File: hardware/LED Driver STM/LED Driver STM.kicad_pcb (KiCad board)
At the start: 2 copper layers, 99 parts, among them J1 I2C4, J2 IO5, J3 PWR, J4 PROG5, J5 ADC2, J6 INT2, J7 INT2, J8 ADC3, Q1 2N7002, Q10 2N7002, Q11 2N7002, Q12 2N7002, Q13 2N7002, Q14 2N7002, Q15 2N7002, Q16 2N7002, Q17 2N7002, Q18 2N7002, Q19 2N7002, Q2 2N7002, Q20 2N7002, Q3 2N7002, Q4 2N7002, Q5 2N7002, Q6 2N7002, Q7 2N7002, Q8 2N7002, Q9 2N7002, SW1 SPT, SW2 SPT, SW3 SPT, U1 STM32F030C8Tx, U2 AMS1117-3.3, U3 L3GD20, U4 LIS3DH, Y1 16MHz

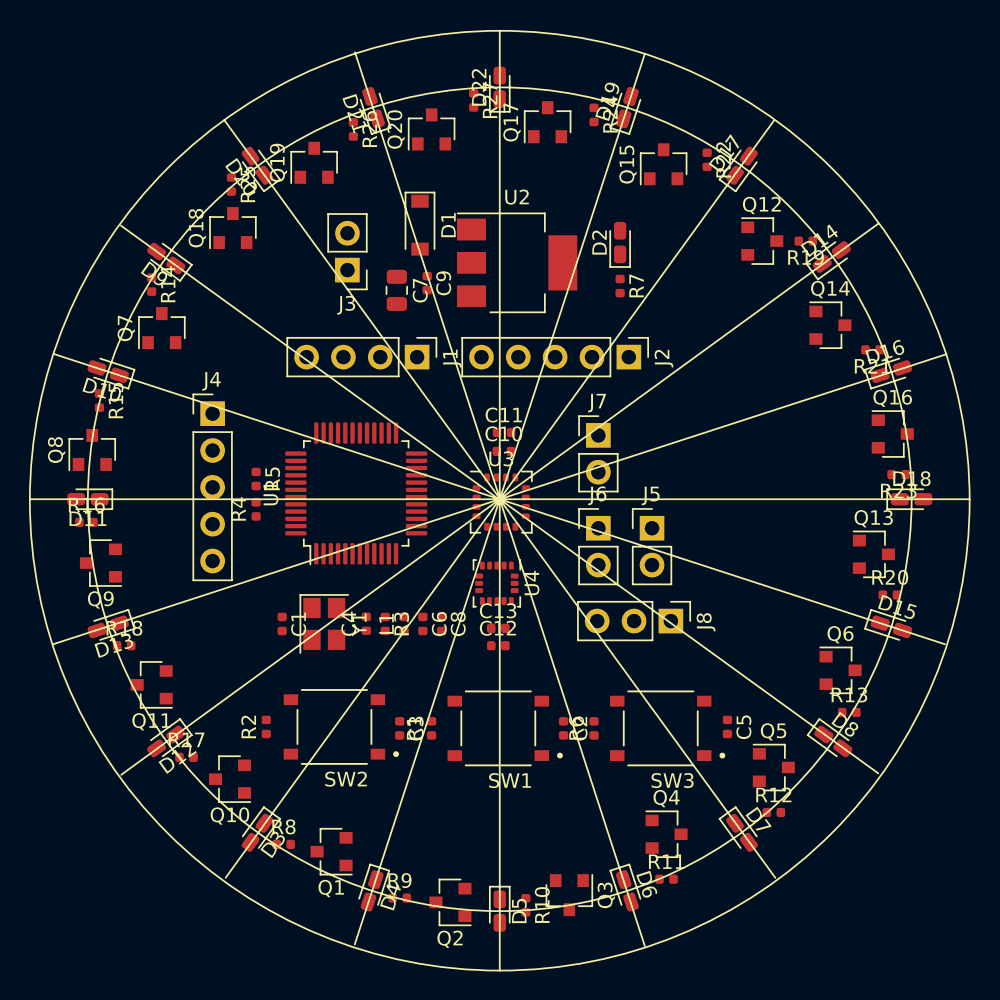
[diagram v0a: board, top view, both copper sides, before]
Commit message: Updated layout
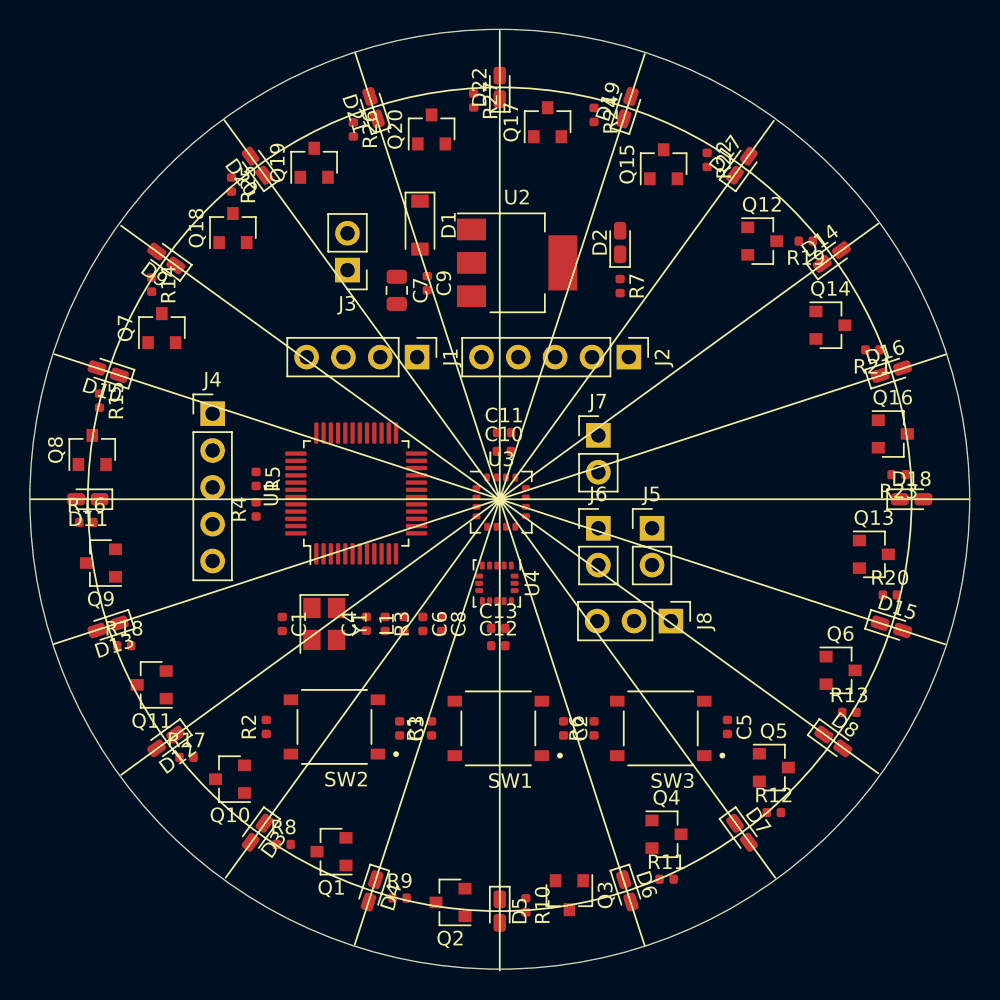
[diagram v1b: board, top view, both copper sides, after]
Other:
- board outline added: 64.8 x 64.8 mm
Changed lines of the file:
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@@
       (outputformat 1)
       (mirror false)
-      (drillshape 1)
+      (drillshape 0)
       (scaleselection 1)
-      (outputdirectory ""))
+      (outputdirectory "gerber/"))
   )
   (net 0 "")
@@
     )
   )
+  (gr_circle (center 120.9 121) (end 153.3 121) (layer Edge.Cuts) (width 0.05))
   (gr_circle (center 120.9 121) (end 120.9 149.4) (layer F.SilkS) (width 0.12))
   (gr_line (start 120.9 121) (end 139.9 147.1) (layer F.SilkS) (width 0.12))
@@
   (gr_line (start 153.3 121) (end 88.5 121) (layer F.SilkS) (width 0.12))
   (gr_line (start 120.9 88.7) (end 120.9 153.5) (layer F.SilkS) (width 0.12))
-  (gr_circle (center 120.9 121.1) (end 153.3 121.3) (layer F.SilkS) (width 0.12))
 )
